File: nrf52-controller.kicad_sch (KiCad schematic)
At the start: 22 parts, among them J1 Conn_01x01_Pin, J2 Conn_01x01_Pin, J3 USB_C_Receptacle_USB2.0, J4 Conn_01x01_Pin, J5 Conn_01x01_Pin, J6 Conn_01x01_Pin, U1 MAX17048G+T10, U10 LSM6DSOX, U6 STWD100YNX

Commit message: schematic rough draft except fpc
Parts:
- added FB1, FB2: FerriteBead_Small, symbol Device:FerriteBead_Small
- added H1, H2: MountingHole_Pad, v12e:MountingHole_1.8mm_M1.6_Pad_TopBottom, symbol Mechanical:MountingHole_Pad
- added U11: USBLC6-2SC6, Package_TO_SOT_SMD:SOT-23-6, symbol Power_Protection:USBLC6-2SC6
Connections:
- net GND: now also H1.1, H2.1, U11.2 (GND)
- net Microcontroller/D+: now also FB2.1; no longer J3.A6 (D+), J3.B6 (D+)
- net Microcontroller/D-: now also FB1.1; no longer J3.A7 (D-), J3.B7 (D-)
- net Power Selection and Regulation/VBUS renamed Microcontroller/VBUS
- net Microcontroller/VBUS: now also U11.5 (VBUS)
- new net: J3.A6 (D+), J3.B6 (D+), U11.3 (I/O2)
- new net: J3.A7 (D-), J3.B7 (D-), U11.1 (I/O1)
- new net: FB1.2, U11.6 (I/O1)
- new net: FB2.2, U11.4 (I/O2)
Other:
- sheet H-Bridge Drivers and FPC ports: added ~{CS0}; removed none
- sheet Microcontroller ports: added VBUS, ~{CS0}; removed none
- note added: "ESD Protection"
- note added: "Mounting Holes"
- note added: "Open-drain output"
- note removed: "Add ESD protection here"
- moved on the sheet: R5, R6

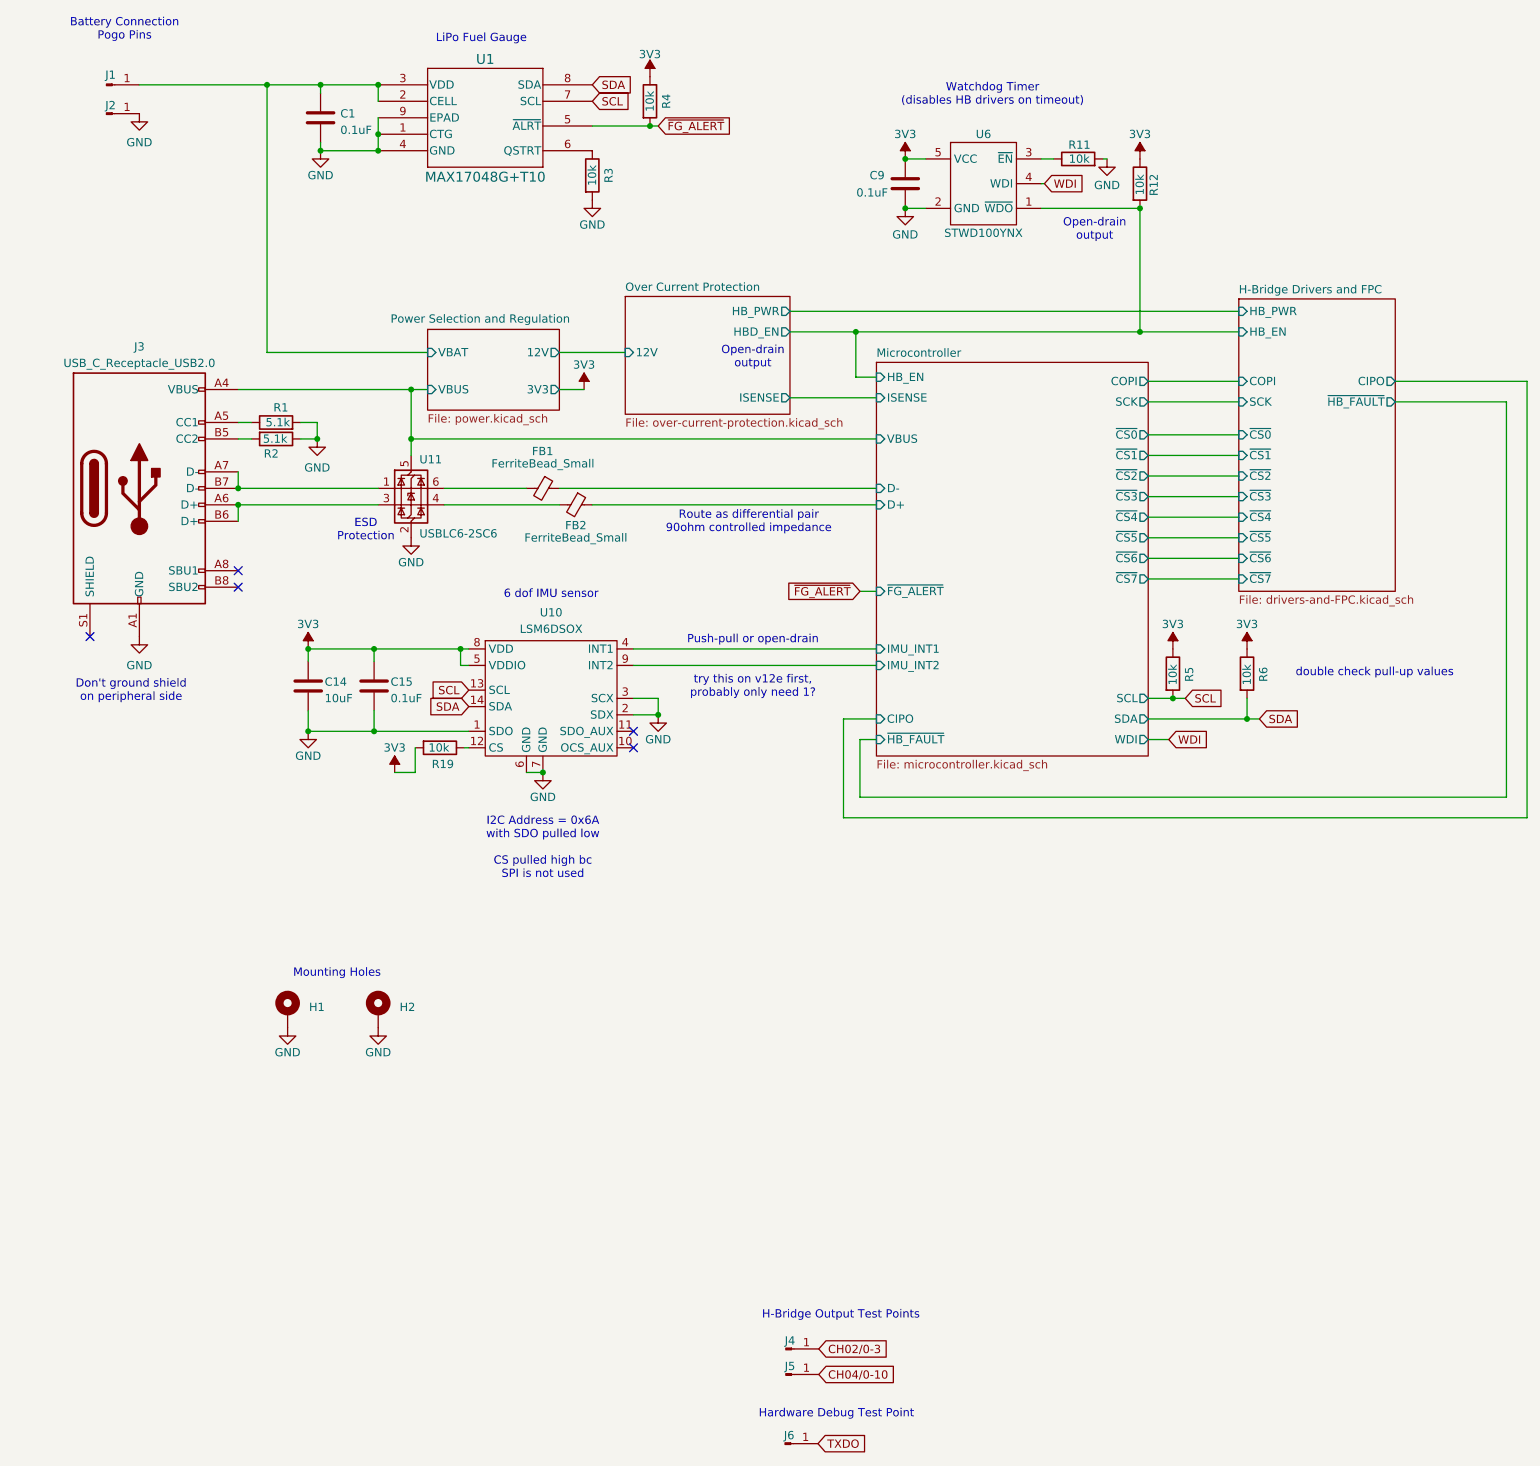
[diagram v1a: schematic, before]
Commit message: schematic draft 2; no FPC connections, no testpoints
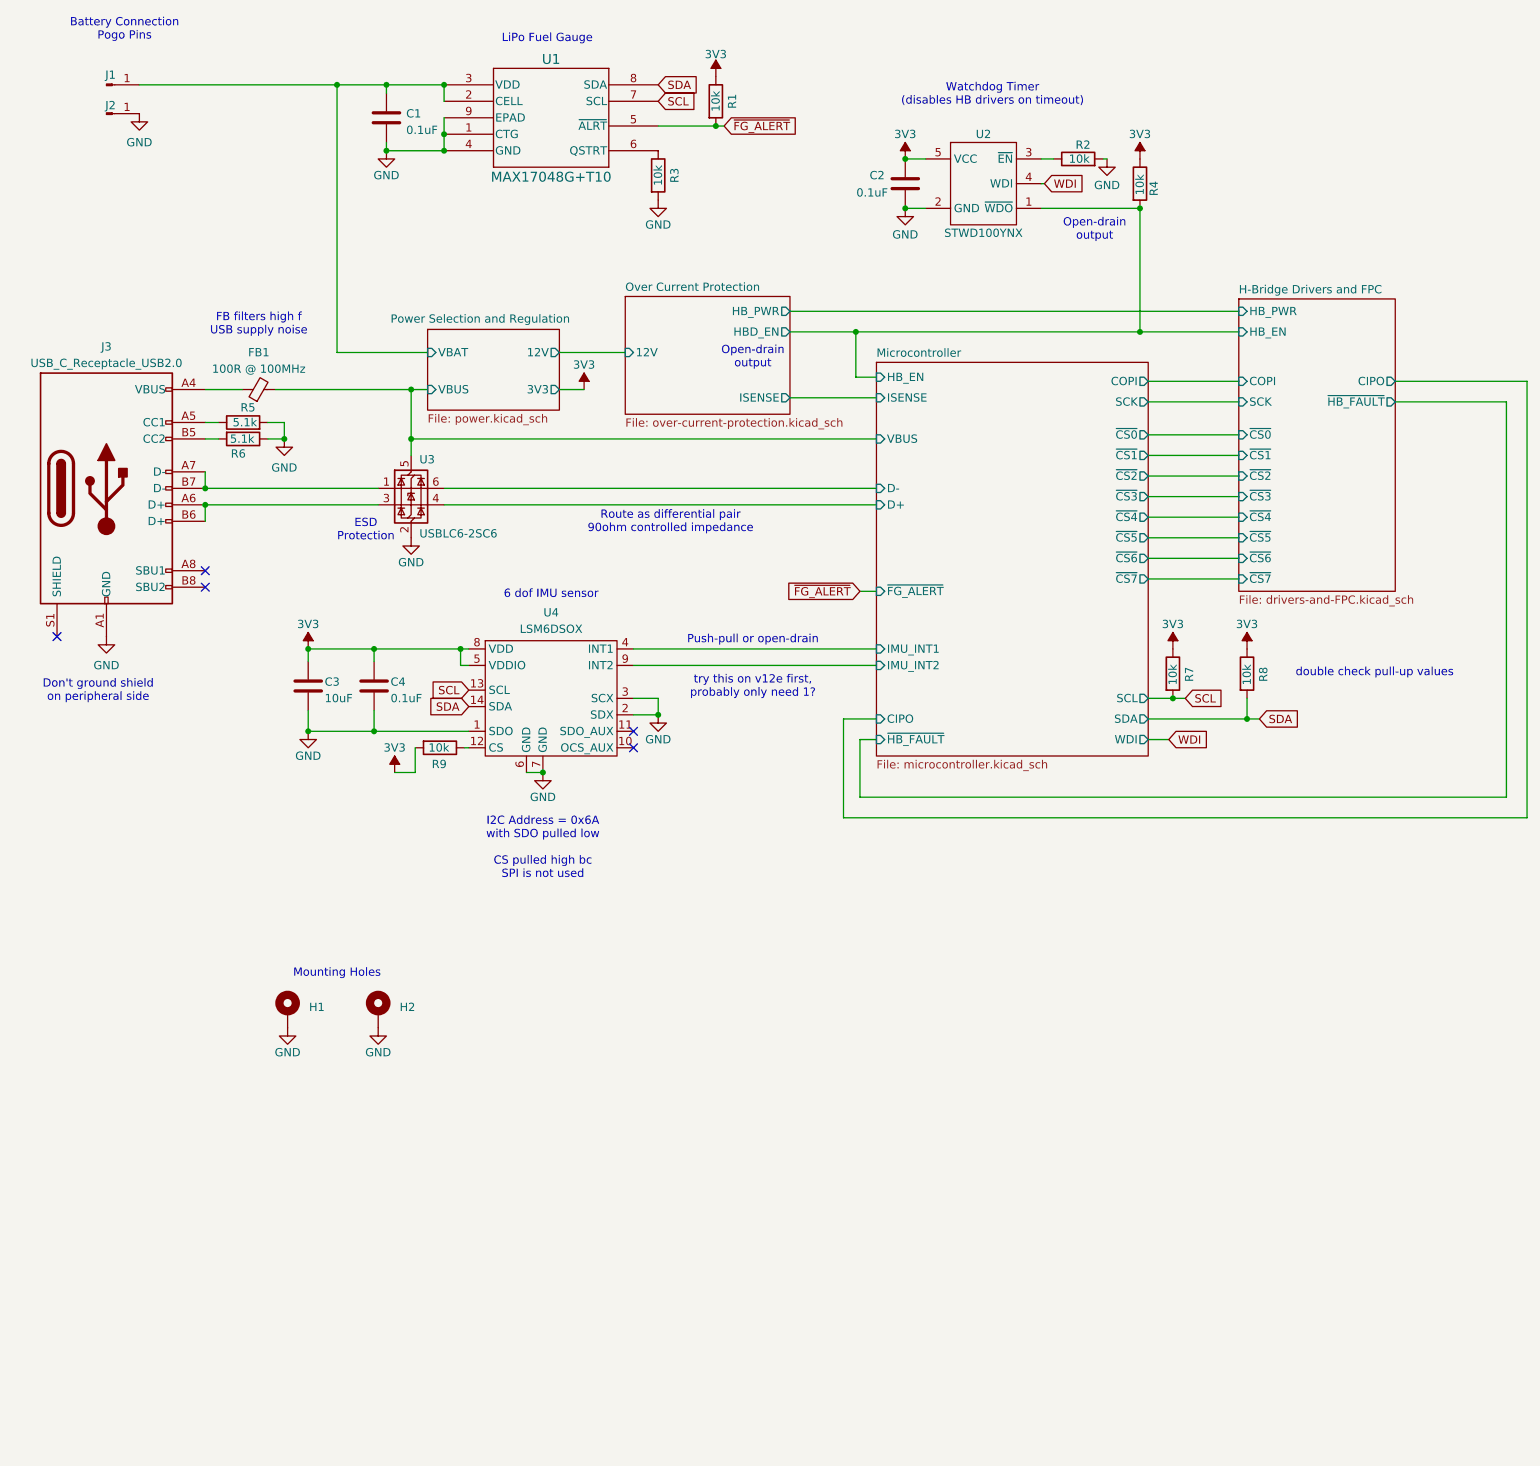
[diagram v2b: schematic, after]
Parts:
- removed FB2: FerriteBead_Small, symbol Device:FerriteBead_Small
- removed J4, J5: Conn_01x01_Pin, v12e:TP_1mm, symbol Connector:Conn_01x01_Pin
- removed J6: Conn_01x01_Pin, v12e:TP_2mm, symbol Connector:Conn_01x01_Pin
- FB1: value FerriteBead_Small -> 100R @ 100MHz; footprint (none) -> Capacitor_SMD:C_0805_2012Metric; JLCPCB Part # (none) -> C1015
- H1, H2: footprint v12e:MountingHole_1.8mm_M1.6_Pad_TopBottom -> nrf52-controller:MountingHole_1.8mm_M1.6_Pad_TopBottom
- J1, J2: footprint v12e:POGO_2mm-base_0.9mm-through-hole -> nrf52-controller:POGO_2mm-base_0.9mm-through-hole
- U1: footprint v12e:21-0168E_T822-3_MXM -> nrf52-controller:21-0168E_T822-3_MXM
- U4: renamed from U10; footprint v12e:LGA-14L_STM -> nrf52-controller:LGA-14L_STM
- renumbered C9 to C2, C14 to C3, C15 to C4, R4 to R1, R11 to R2, R12 to R4, R1 to R5, R2 to R6, R5 to R7, R6 to R8, R19 to R9, U6 to U2, U11 to U3
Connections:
- net Microcontroller/D+: now also U3.4 (I/O2)
- net Microcontroller/D-: now also U3.6 (I/O1); no longer FB1.1
- net Microcontroller/VBUS: now also FB1.2; no longer J3.A4 (VBUS), J3.A9 (VBUS), J3.B4 (VBUS), J3.B9 (VBUS)
- new net: FB1.1, J3.A4 (VBUS), J3.A9 (VBUS), J3.B4 (VBUS), J3.B9 (VBUS)
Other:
- note added: "FB filters high f USB supply noise"
- note removed: "H-Bridge Output Test Points"
- note removed: "Hardware Debug Test Point"
- moved on the sheet: C1, J3, R1, R3, R5, R6, U1

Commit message: layout start
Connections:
- net VBUS_IN: now reaches FB1.1, J3.A4 (VBUS), J3.A9 (VBUS), J3.B4 (VBUS), J3.B9 (VBUS)
- net CC1: now reaches J3.A5 (CC1), R5.1
- net D+_IN: now reaches J3.A6 (D+), J3.B6 (D+), U3.3 (I/O2)
- net D-_IN: now reaches J3.A7 (D-), J3.B7 (D-), U3.1 (I/O1)
- net CC2: now reaches J3.B5 (CC2), R6.2
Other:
- sheet Microcontroller ports: added 12V_EN1; removed none
- sheet Power Selection and Regulation ports: added 12V_EN1; removed none
- moved on the sheet: FB1, R5, R6
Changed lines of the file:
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@@
 	)
 	(junction
-		(at 58.547 86.995)
+		(at 62.865 86.995)
 		(diameter 0)
 		(color 0 0 0 0)
@@
 	(wire
 		(pts
+			(xy 71.755 76.2) (xy 80.645 76.2)
+		)
+		(stroke
+			(width 0)
+			(type default)
+		)
+	)
+	(wire
+		(pts
 			(xy 74.295 41.275) (xy 74.295 42.545)
 		)
@@
 	(wire
 		(pts
-			(xy 58.547 84.455) (xy 58.547 86.995)
+			(xy 62.865 84.455) (xy 62.865 86.995)
 		)
 		(stroke
@@
 	(wire
 		(pts
-			(xy 57.15 79.375) (xy 78.105 79.375)
+			(xy 63.5 79.375) (xy 78.105 79.375)
 		)
 		(stroke
@@
 	(wire
 		(pts
-			(xy 66.675 73.66) (xy 80.645 73.66)
+			(xy 66.675 73.025) (xy 80.645 73.025)
 		)
 		(stroke
@@
 	(wire
 		(pts
-			(xy 46.355 84.455) (xy 48.387 84.455)
+			(xy 46.355 84.455) (xy 52.705 84.455)
 		)
 		(stroke
@@
 	(wire
 		(pts
-			(xy 56.007 86.995) (xy 58.547 86.995)
+			(xy 60.325 86.995) (xy 62.865 86.995)
 		)
 		(stroke
@@
 	(wire
 		(pts
+			(xy 191.77 111.76) (xy 201.295 111.76)
+		)
+		(stroke
+			(width 0)
+			(type default)
+		)
+	)
+	(wire
+		(pts
 			(xy 100.965 79.375) (xy 104.775 79.375)
 		)
@@
 	(wire
 		(pts
-			(xy 56.007 84.455) (xy 58.547 84.455)
+			(xy 60.325 84.455) (xy 62.865 84.455)
 		)
 		(stroke
@@
 	(wire
 		(pts
-			(xy 46.355 79.375) (xy 52.07 79.375)
+			(xy 46.355 79.375) (xy 58.42 79.375)
 		)
 		(stroke
@@
 	(wire
 		(pts
-			(xy 46.355 86.995) (xy 48.387 86.995)
+			(xy 46.355 86.995) (xy 52.705 86.995)
 		)
 		(stroke
@@
 	(wire
 		(pts
-			(xy 66.675 73.66) (xy 66.675 32.385)
+			(xy 66.675 73.025) (xy 66.675 32.385)
 		)
 		(stroke
@@
 		)
 	)
+	(label "CC2"
+		(at 46.355 86.995 0)
+		(fields_autoplaced yes)
+		(effects
+			(font
+				(size 1.27 1.27)
+			)
+			(justify left bottom)
+		)
+	)
+	(label "VBUS_IN"
+		(at 46.355 79.375 0)
+		(fields_autoplaced yes)
+		(effects
+			(font
+				(size 1.27 1.27)
+			)
+			(justify left bottom)
+		)
+	)
+	(label "D+_IN"
+		(at 46.355 97.155 0)
+		(fields_autoplaced yes)
+		(effects
+			(font
+				(size 1.27 1.27)
+			)
+			(justify left bottom)
+		)
+	)
+	(label "CC1"
+		(at 46.355 84.455 0)
+		(fields_autoplaced yes)
+		(effects
+			(font
+				(size 1.27 1.27)
+			)
+			(justify left bottom)
+		)
+	)
+	(label "12V_EN1"
+		(at 201.295 111.76 180)
+		(fields_autoplaced yes)
+		(effects
+			(font
+				(size 1.27 1.27)
+			)
+			(justify right bottom)
+		)
+	)
+	(label "12V_EN1"
+		(at 71.755 76.2 0)
+		(fields_autoplaced yes)
+		(effects
+			(font
+				(size 1.27 1.27)
+			)
+			(justify left bottom)
+		)
+	)
+	(label "D-_IN"
+		(at 46.355 94.615 0)
+		(fields_autoplaced yes)
+		(effects
+			(font
+				(size 1.27 1.27)
+			)
+			(justify left bottom)
+		)
+	)
 	(global_label "SDA"
 		(shape input)
@@
 	(symbol
 		(lib_id "Device:R")
-		(at 52.197 86.995 270)
+		(at 56.515 86.995 270)
 		(unit 1)
 		(exclude_from_sim no)
@@
 		(dnp no)
 		(property "Reference" "R6"
-			(at 50.292 89.281 90)
+			(at 54.61 89.281 90)
 			(effects
 				(font
@@
 		)
 		(property "Value" "5.1k"
-			(at 50.165 86.995 90)
+			(at 54.483 86.995 90)
 			(effects
 				(font
@@
 		)
 		(property "Footprint" "Resistor_SMD:R_0402_1005Metric"
-			(at 52.197 85.217 90)
+			(at 56.515 85.217 90)
 			(effects
 				(font
@@
 		)
 		(property "Datasheet" "~"
-			(at 52.197 86.995 0)
+			(at 56.515 86.995 0)
 			(effects
 				(font
@@
 		)
 		(property "Description" ""
-			(at 52.197 86.995 0)
+			(at 56.515 86.995 0)
 			(effects
 				(font
@@
 		)
 		(property "JLCPCB Part #" "C25905"
-			(at 52.197 86.995 90)
+			(at 56.515 86.995 90)
 			(effects
 				(font
@@
 	(symbol
 		(lib_id "Device:R")
-		(at 52.197 84.455 90)
+		(at 56.515 84.455 90)
 		(unit 1)
 		(exclude_from_sim no)
@@
 		(dnp no)
 		(property "Reference" "R5"
-			(at 54.102 82.169 90)
+			(at 58.42 82.169 90)
 			(effects
 				(font
@@
 		)
 		(property "Value" "5.1k"
-			(at 54.356 84.455 90)
+			(at 58.674 84.455 90)
 			(effects
 				(font
@@
 		)
 		(property "Footprint" "Resistor_SMD:R_0402_1005Metric"
-			(at 52.197 86.233 90)
+			(at 56.515 86.233 90)
 			(effects
 				(font
@@
 		)
 		(property "Datasheet" "~"
-			(at 52.197 84.455 0)
+			(at 56.515 84.455 0)
 			(effects
 				(font
@@
 		)
 		(property "Description" ""
-			(at 52.197 84.455 0)
+			(at 56.515 84.455 0)
 			(effects
 				(font
@@
 		)
 		(property "JLCPCB Part #" "C25905"
-			(at 52.197 84.455 90)
+			(at 56.515 84.455 90)
 			(effects
 				(font
@@
 	(symbol
 		(lib_id "Device:FerriteBead_Small")
-		(at 54.61 79.375 90)
+		(at 60.96 79.375 90)
 		(unit 1)
 		(exclude_from_sim no)
@@
 		(dnp no)
 		(property "Reference" "FB1"
-			(at 54.61 73.66 90)
+			(at 60.96 73.66 90)
 			(effects
 				(font
@@
 		)
 		(property "Value" "100R @ 100MHz"
-			(at 54.61 76.2 90)
+			(at 60.96 75.565 90)
 			(effects
 				(font
@@
 		)
 		(property "Footprint" "Capacitor_SMD:C_0805_2012Metric"
-			(at 54.61 81.153 90)
+			(at 60.96 81.153 90)
 			(effects
 				(font
@@
 		)
 		(property "Datasheet" "~"
-			(at 54.61 79.375 0)
+			(at 60.96 79.375 0)
 			(effects
 				(font
@@
 		)
 		(property "Description" "Ferrite bead, small symbol"
-			(at 54.61 79.375 0)
+			(at 60.96 79.375 0)
 			(effects
 				(font
@@
 		)
 		(property "JLCPCB Part #" "C1015"
-			(at 54.61 79.375 90)
+			(at 60.96 79.375 90)
 			(effects
 				(font
@@
 	(symbol
 		(lib_id "power:GND")
-		(at 58.547 86.995 0)
+		(at 62.865 86.995 0)
 		(unit 1)
 		(exclude_from_sim no)
@@
 		(dnp no)
 		(property "Reference" "#PWR010"
-			(at 58.547 93.345 0)
+			(at 62.865 93.345 0)
 			(effects
 				(font
@@
 		)
 		(property "Value" "GND"
-			(at 58.547 91.44 0)
+			(at 62.865 91.44 0)
 			(effects
 				(font
@@
 		)
 		(property "Footprint" ""
-			(at 58.547 86.995 0)
+			(at 62.865 86.995 0)
 			(effects
 				(font
@@
 		)
 		(property "Datasheet" ""
-			(at 58.547 86.995 0)
+			(at 62.865 86.995 0)
 			(effects
 				(font
@@
 		)
 		(property "Description" ""
-			(at 58.547 86.995 0)
+			(at 62.865 86.995 0)
 			(effects
 				(font
@@
 		)
 		(pin "VBAT" input
-			(at 80.645 73.66 180)
+			(at 80.645 73.025 180)
 			(effects
 				(font
@@
 			)
 		)
+		(pin "12V_EN1" input
+			(at 80.645 76.2 180)
+			(effects
+				(font
+					(size 1.27 1.27)
+				)
+				(justify left)
+			)
+		)
 		(instances
 			(project "nrf52-controller"
@@
 			)
 		)
+		(pin "12V_EN1" output
+			(at 191.77 111.76 0)
+			(effects
+				(font
+					(size 1.27 1.27)
+				)
+				(justify right)
+			)
+		)
